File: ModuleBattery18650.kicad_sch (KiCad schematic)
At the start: 28 parts, among them J1 Connector_6p, T1 SI2323DS-T1-E3, T2 FDN337N, T3 SI2323DS-T1-E3, U1 MCP73832-2-OT, U2 MCP121T-315E

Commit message: Changes
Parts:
- removed C1: 4.7uF, 0ESN_Lib:C_0805_2012Metric_Pad1.18x1.45mm_HandSolder, symbol Device:C
- removed D1: LED 2V, 0ESN_Lib:D_0603_1608Metric_Pad1.05x0.95mm_HandSolder, symbol Device:LED
- removed JP1, JP2: Jumper_2_Bridged, 0ESN_Lib:PinHeader_1x02_P1.27mm_Vertical, symbol 0ESN_Lib:Jumper_2_Bridged
- removed R2: 1k8, 0ESN_Lib:R_0603_1608Metric_Pad0.98x0.95mm_HandSolder, symbol Device:R
- removed R3: 4k7, 0ESN_Lib:R_0603_1608Metric_Pad0.98x0.95mm_HandSolder, symbol Device:R
- removed U1: MCP73832-2-OT, 0ESN_Lib:SOT-23-5_HandSoldering, symbol 0ESN_Lib:MCP73832-2-OT
- added RS1: 0R NP, 0ESN_Lib:R_0603_1608Metric_Pad0.98x0.95mm_HandSolder, symbol Device:R
- added T1, T2: SI2323DS, Package_TO_SOT_SMD:SOT-23_Handsoldering, symbol 0ESN_Lib:SI2323DS
- added TP9: TestPoint, 0ESN_Lib:TestPoint_Pad_D1.0mm, symbol 0ESN_Lib:TestPoint
- R1: value 3k9 -> 1M
- T4: renamed from T3; value SI2323DS-T1-E3 -> SI2323DS; symbol 0ESN_Lib:SI2323DS-T1-E3 -> 0ESN_Lib:SI2323DS
- T5: renamed from T1; value SI2323DS-T1-E3 -> SI2323DS; symbol 0ESN_Lib:SI2323DS-T1-E3 -> 0ESN_Lib:SI2323DS
- renumbered C2 to C1, JP3 to JP1, R4 to R2, R5 to R3, R6 to RS2, T2 to T3, TP4 to TP2, TP2 to TP4, U2 to U1
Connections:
- net VDD is gone; now on an unnamed net: JP1.2 (B), TP3.1
- net GND: now also T1.1 (G)
- net Vbat: now also T5.2 (S), TP9.1; no longer RS2.2, T4.3 (D), TP8.1
- net at R2.1, R3.1, RS2.1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: now also RS1.2, T2.3 (D); no longer T5.2 (S)
- net at R1.1: now also T1.3 (D), T2.1 (G)
- net Vcharge: no longer names the net of C1.1, F1.2, TP4.1
- net Vcharge: now also RS1.1, T1.2 (S), T2.2 (S); no longer T5.3 (D)
- new net: RS2.2, T4.3 (D), T5.3 (D), TP8.1
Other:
- note added: "Bypass resistor"
- note added: "Disable subcircuit when charging"
- note added: "Prevent over-discharge"
- note added: "Prevent reverse current"
- note added: "Replace with different pins one 1x Vbat 1x Vcharge 1x GND"
- note added: "Using 3 P-Channel mosfet adds a serial resistor to the battery The SI2323DS has a Rds_on of about 39 mOhm with this voltage A better one like the SI7145DP has a Rds_on of up to 6 mOhm for 3V Or the SISH615ADN for a cheaper alternative, Rds_on up to 8 mOhm A serial resistance of 120 mOhm would mean that drawing 1 Amp from the current source, 120mW is dissiped into the mosfets"
- note added: "When over-discharge disabled : MCP121T consumes 1.75 uA R1 draws nothing R2 draws nothing R3 draws 3.08 uA Total is around 5 uA"
- note added: "When over-discharge enabled : MCP121T consumes 1.75 uA R1 draws nothing R2 draws 3.08 uA (for 1 Mohm, need to verify that is enough to pull up T3) R3 draws nothing as the gate of T4 is High Total is around 5 uA"
- note removed: "256mA"
- note removed: "555mA"
- note removed: "Ich = 1000V/Rch [A]"
- moved on the sheet: J1, JP1, R2, R3, RS2, T3, T4, T5, TP1, TP2, TP3, TP4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

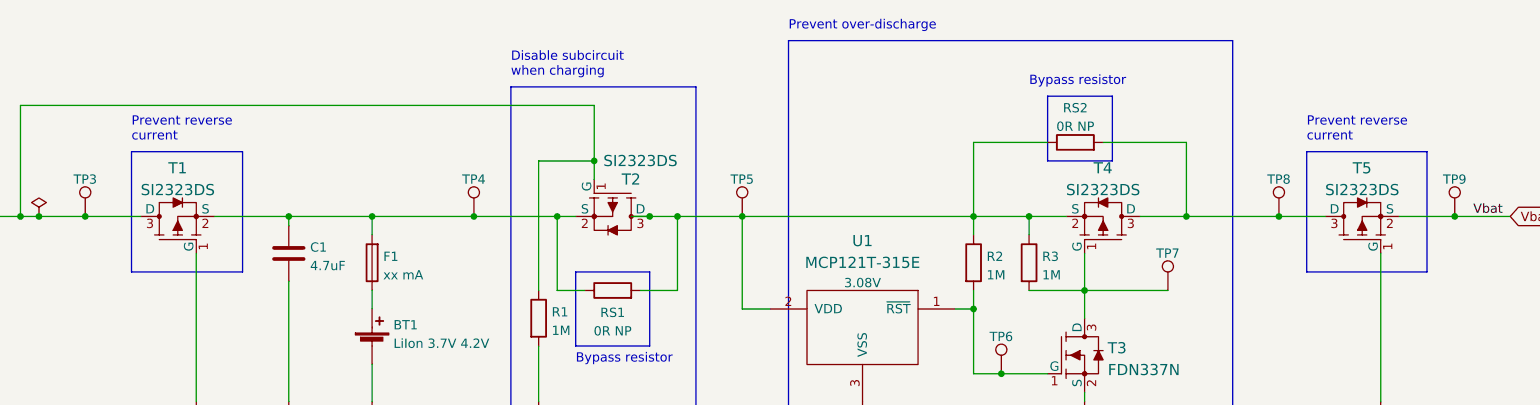
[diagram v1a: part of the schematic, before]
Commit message: corrected mosfet model
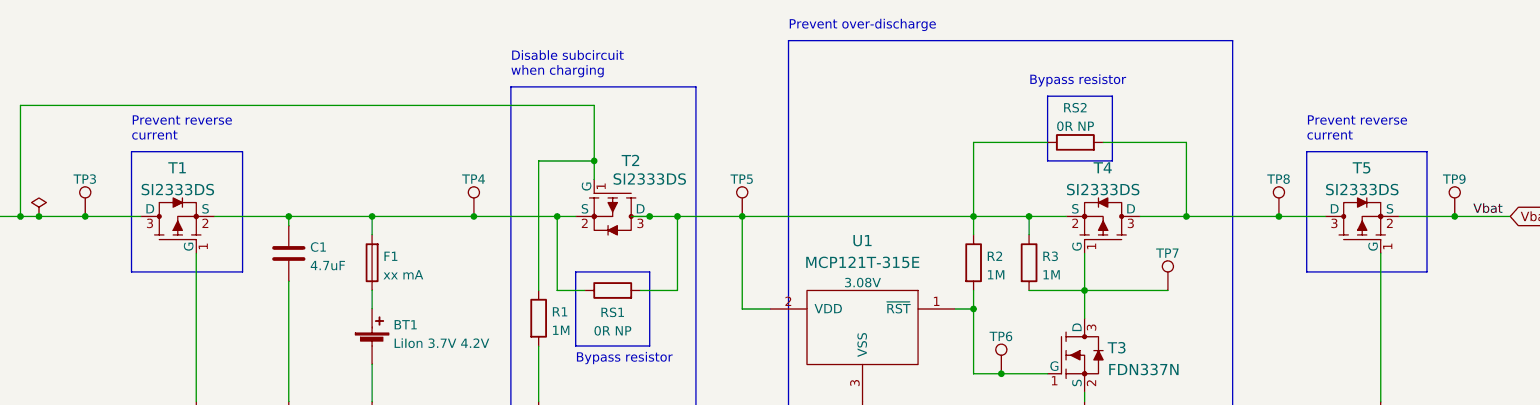
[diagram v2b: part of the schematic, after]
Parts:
- T1, T2, T4, T5: value SI2323DS -> SI2333DS; symbol 0ESN_Lib:SI2323DS -> 0ESN_Lib:SI2333DS
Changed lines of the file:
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@@
   (symbol (lib_id "power:GND") (at 256.54 83.82 0) (unit 1)
     (in_bom yes) (on_board yes) (fields_autoplaced)
-    (property "Reference" "#PWR010" (id 0) (at 256.54 90.17 0)
+    (property "Reference" "#PWR08" (id 0) (at 256.54 90.17 0)
       (effects (font (size 1.27 1.27)) hide)
     )
@@
     (pin "1")
   )
-  (symbol (lib_id "0ESN_Lib:SI2323DS") (at 91.44 58.42 0) (unit 1)
+  (symbol (lib_id "0ESN_Lib:SI2333DS") (at 91.44 58.42 0) (unit 1)
     (in_bom yes) (on_board yes) (fields_autoplaced)
     (property "Reference" "T1" (id 0) (at 91.44 51.7959 0)
       (effects (font (size 1.524 1.524)))
     )
-    (property "Value" "SI2323DS" (id 1) (at 91.44 54.7893 0)
+    (property "Value" "SI2333DS" (id 1) (at 91.44 54.7893 0)
       (effects (font (size 1.524 1.524)))
     )
@@
       (effects (font (size 1.524 1.524)) hide)
     )
-    (property "Datasheet" "" (id 3) (at 91.44 59.055 0)
+    (property "Datasheet" "https://www.vishay.com/docs/72023/72023.pdf" (id 3) (at 91.44 59.055 0)
       (effects (font (size 1.524 1.524)) hide)
     )
@@
   (symbol (lib_id "power:GND") (at 93.98 83.82 0) (unit 1)
     (in_bom yes) (on_board yes) (fields_autoplaced)
-    (property "Reference" "#PWR03" (id 0) (at 93.98 90.17 0)
+    (property "Reference" "#PWR02" (id 0) (at 93.98 90.17 0)
       (effects (font (size 1.27 1.27)) hide)
     )
@@
     (pin "1")
   )
-  (symbol (lib_id "0ESN_Lib:SI2323DS") (at 151.13 58.42 180) (unit 1)
+  (symbol (lib_id "0ESN_Lib:SI2333DS") (at 151.13 58.42 180) (unit 1)
     (in_bom yes) (on_board yes)
-    (property "Reference" "T2" (id 0) (at 153.67 53.34 0)
-      (effects (font (size 1.524 1.524)))
-    )
-    (property "Value" "SI2323DS" (id 1) (at 154.94 50.8 0)
+    (property "Reference" "T2" (id 0) (at 153.67 50.8 0)
+      (effects (font (size 1.524 1.524)))
+    )
+    (property "Value" "SI2333DS" (id 1) (at 156.21 53.34 0)
       (effects (font (size 1.524 1.524)))
     )
@@
       (effects (font (size 1.524 1.524)) hide)
     )
-    (property "Datasheet" "" (id 3) (at 151.13 57.785 0)
+    (property "Datasheet" "https://www.vishay.com/docs/72023/72023.pdf" (id 3) (at 151.13 57.785 0)
       (effects (font (size 1.524 1.524)) hide)
     )
@@
     (pin "1")
   )
-  (symbol (lib_id "0ESN_Lib:SI2323DS") (at 254 58.42 0) (unit 1)
+  (symbol (lib_id "0ESN_Lib:SI2333DS") (at 254 58.42 0) (unit 1)
     (in_bom yes) (on_board yes) (fields_autoplaced)
     (property "Reference" "T5" (id 0) (at 254 51.7959 0)
       (effects (font (size 1.524 1.524)))
     )
-    (property "Value" "SI2323DS" (id 1) (at 254 54.7893 0)
+    (property "Value" "SI2333DS" (id 1) (at 254 54.7893 0)
       (effects (font (size 1.524 1.524)))
     )
@@
       (effects (font (size 1.524 1.524)) hide)
     )
-    (property "Datasheet" "" (id 3) (at 254 59.055 0)
+    (property "Datasheet" "https://www.vishay.com/docs/72023/72023.pdf" (id 3) (at 254 59.055 0)
       (effects (font (size 1.524 1.524)) hide)
     )
@@
   (symbol (lib_id "power:GND") (at 140.97 83.82 0) (unit 1)
     (in_bom yes) (on_board yes) (fields_autoplaced)
-    (property "Reference" "#PWR06" (id 0) (at 140.97 90.17 0)
+    (property "Reference" "#PWR05" (id 0) (at 140.97 90.17 0)
       (effects (font (size 1.27 1.27)) hide)
     )
@@
   (symbol (lib_id "power:GND") (at 106.68 83.82 0) (unit 1)
     (in_bom yes) (on_board yes) (fields_autoplaced)
-    (property "Reference" "#PWR04" (id 0) (at 106.68 90.17 0)
+    (property "Reference" "#PWR03" (id 0) (at 106.68 90.17 0)
       (effects (font (size 1.27 1.27)) hide)
     )
@@
   (symbol (lib_id "power:GND") (at 215.9 83.82 0) (unit 1)
     (in_bom yes) (on_board yes) (fields_autoplaced)
-    (property "Reference" "#PWR09" (id 0) (at 215.9 90.17 0)
+    (property "Reference" "#PWR07" (id 0) (at 215.9 90.17 0)
       (effects (font (size 1.27 1.27)) hide)
     )
@@
   (symbol (lib_id "power:GND") (at 185.42 83.82 0) (unit 1)
     (in_bom yes) (on_board yes) (fields_autoplaced)
-    (property "Reference" "#PWR08" (id 0) (at 185.42 90.17 0)
+    (property "Reference" "#PWR06" (id 0) (at 185.42 90.17 0)
       (effects (font (size 1.27 1.27)) hide)
     )
@@
   (symbol (lib_id "power:GND") (at 118.11 83.82 0) (unit 1)
     (in_bom yes) (on_board yes) (fields_autoplaced)
-    (property "Reference" "#PWR05" (id 0) (at 118.11 90.17 0)
+    (property "Reference" "#PWR04" (id 0) (at 118.11 90.17 0)
       (effects (font (size 1.27 1.27)) hide)
     )
@@
     (pin "1")
   )
-  (symbol (lib_id "0ESN_Lib:SI2323DS") (at 218.44 58.42 0) (mirror y) (unit 1)
+  (symbol (lib_id "0ESN_Lib:SI2333DS") (at 218.44 58.42 0) (mirror y) (unit 1)
     (in_bom yes) (on_board yes) (fields_autoplaced)
     (property "Reference" "T4" (id 0) (at 218.44 51.7959 0)
       (effects (font (size 1.524 1.524)))
     )
-    (property "Value" "SI2323DS" (id 1) (at 218.44 54.7893 0)
+    (property "Value" "SI2333DS" (id 1) (at 218.44 54.7893 0)
       (effects (font (size 1.524 1.524)))
     )
@@
       (effects (font (size 1.524 1.524)) hide)
     )
-    (property "Datasheet" "" (id 3) (at 218.44 59.055 0)
+    (property "Datasheet" "https://www.vishay.com/docs/72023/72023.pdf" (id 3) (at 218.44 59.055 0)
       (effects (font (size 1.524 1.524)) hide)
     )
@@
     )
     (path "/23b85cef-66d9-43b8-b31f-1044e0d3ebc7"
+      (reference "#PWR02") (unit 1) (value "GND") (footprint "")
+    )
+    (path "/a1c2006c-9990-442c-88d7-ddca560a04cd"
       (reference "#PWR03") (unit 1) (value "GND") (footprint "")
     )
-    (path "/a1c2006c-9990-442c-88d7-ddca560a04cd"
+    (path "/e065cd76-3830-4be0-892c-04089454b25f"
       (reference "#PWR04") (unit 1) (value "GND") (footprint "")
     )
-    (path "/e065cd76-3830-4be0-892c-04089454b25f"
+    (path "/60ef1753-16ee-40fd-a34a-5fee75f98232"
       (reference "#PWR05") (unit 1) (value "GND") (footprint "")
     )
-    (path "/60ef1753-16ee-40fd-a34a-5fee75f98232"
+    (path "/cfa2cdea-57ac-4cf2-a8c7-f359f96a51ae"
       (reference "#PWR06") (unit 1) (value "GND") (footprint "")
     )
-    (path "/cfa2cdea-57ac-4cf2-a8c7-f359f96a51ae"
+    (path "/c5589686-1dea-4bbf-935c-6a54f89cec88"
+      (reference "#PWR07") (unit 1) (value "GND") (footprint "")
+    )
+    (path "/0fa377f7-81c1-4b1f-8399-5259acb98d09"
       (reference "#PWR08") (unit 1) (value "GND") (footprint "")
-    )
-    (path "/c5589686-1dea-4bbf-935c-6a54f89cec88"
-      (reference "#PWR09") (unit 1) (value "GND") (footprint "")
-    )
-    (path "/0fa377f7-81c1-4b1f-8399-5259acb98d09"
-      (reference "#PWR010") (unit 1) (value "GND") (footprint "")
     )
     (path "/3563b52b-d2c0-41b9-aeca-2af682e9e33e"
@@
     )
     (path "/1faa3af5-61f3-4f40-a3ca-42ba69cf237c"
-      (reference "T1") (unit 1) (value "SI2323DS") (footprint "Package_TO_SOT_SMD:SOT-23_Handsoldering")
+      (reference "T1") (unit 1) (value "SI2333DS") (footprint "Package_TO_SOT_SMD:SOT-23_Handsoldering")
     )
     (path "/314eb51e-b3ac-4ba9-8b88-2b7ab2de42c3"
-      (reference "T2") (unit 1) (value "SI2323DS") (footprint "Package_TO_SOT_SMD:SOT-23_Handsoldering")
+      (reference "T2") (unit 1) (value "SI2333DS") (footprint "Package_TO_SOT_SMD:SOT-23_Handsoldering")
     )
     (path "/78dd3410-41be-43bf-b6a5-ead893855ad4"
@@
     )
     (path "/f948391d-3a89-47b0-b2ec-af1ff0696bd4"
-      (reference "T4") (unit 1) (value "SI2323DS") (footprint "Package_TO_SOT_SMD:SOT-23_Handsoldering")
+      (reference "T4") (unit 1) (value "SI2333DS") (footprint "Package_TO_SOT_SMD:SOT-23_Handsoldering")
     )
     (path "/57796aa7-6c40-491b-8224-cb866b640d9f"
-      (reference "T5") (unit 1) (value "SI2323DS") (footprint "Package_TO_SOT_SMD:SOT-23_Handsoldering")
+      (reference "T5") (unit 1) (value "SI2333DS") (footprint "Package_TO_SOT_SMD:SOT-23_Handsoldering")
     )
     (path "/fec7520f-6d3f-4e1d-a13a-d895d7868e2f"

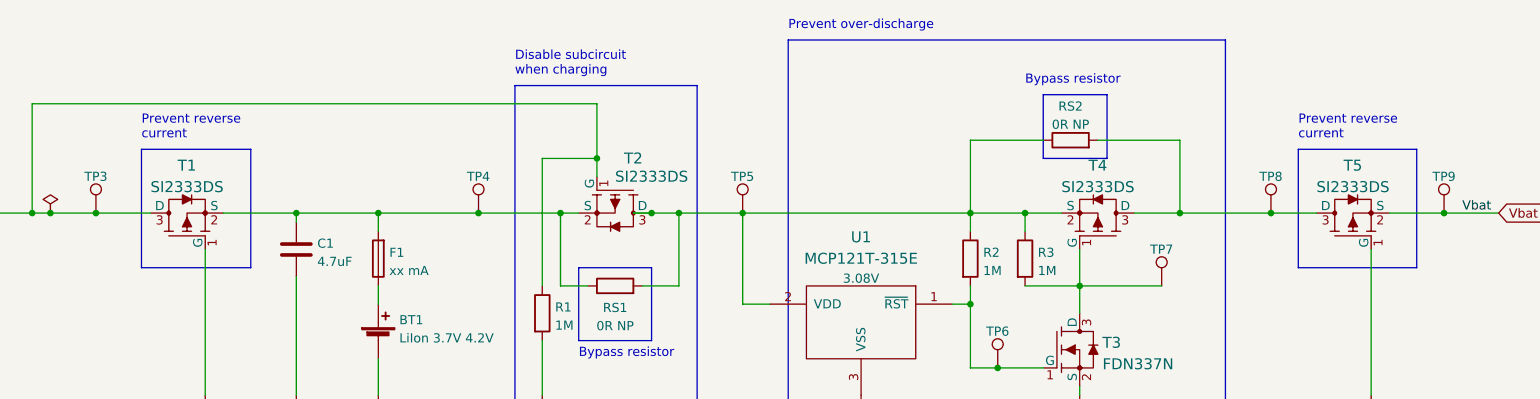
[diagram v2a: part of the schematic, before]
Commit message: Changed mosfets models to SISH615ADN
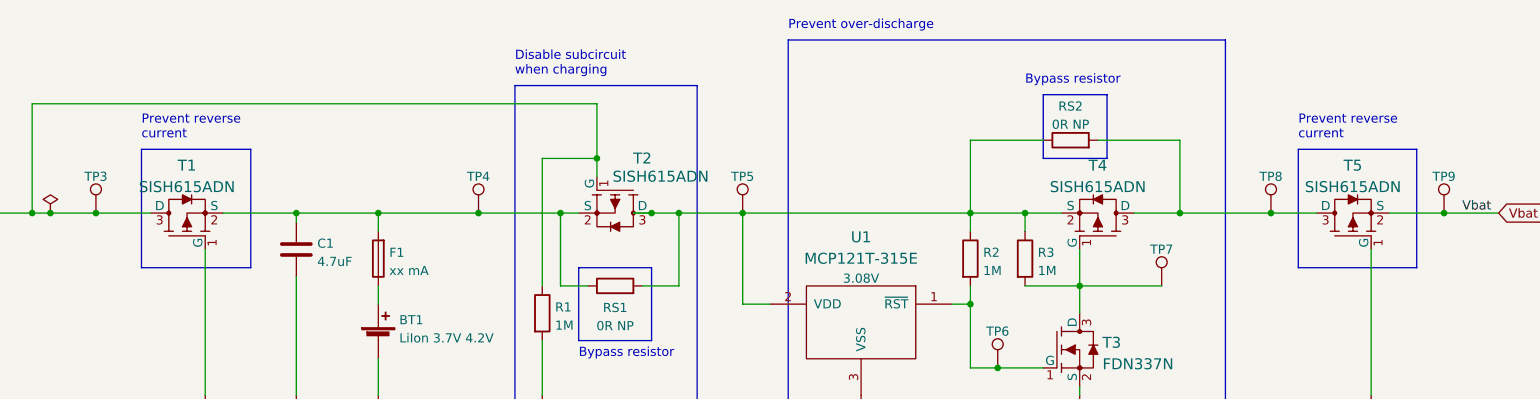
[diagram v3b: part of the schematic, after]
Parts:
- T1, T2, T4, T5: value SI2333DS -> SISH615ADN; footprint Package_TO_SOT_SMD:SOT-23_Handsoldering -> 0ESN_Lib:PowerPAK 1212-8S; symbol 0ESN_Lib:SI2333DS -> 0ESN_Lib:SISH615ADN
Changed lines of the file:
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@@
     (pin "1")
   )
-  (symbol (lib_id "0ESN_Lib:SI2333DS") (at 91.44 58.42 0) (unit 1)
+  (symbol (lib_id "0ESN_Lib:SISH615ADN") (at 91.44 58.42 0) (unit 1)
     (in_bom yes) (on_board yes) (fields_autoplaced)
     (property "Reference" "T1" (id 0) (at 91.44 51.7959 0)
       (effects (font (size 1.524 1.524)))
     )
-    (property "Value" "SI2333DS" (id 1) (at 91.44 54.7893 0)
-      (effects (font (size 1.524 1.524)))
-    )
-    (property "Footprint" "Package_TO_SOT_SMD:SOT-23_Handsoldering" (id 2) (at 91.44 59.055 0)
+    (property "Value" "SISH615ADN" (id 1) (at 91.44 54.7893 0)
+      (effects (font (size 1.524 1.524)))
+    )
+    (property "Footprint" "0ESN_Lib:PowerPAK 1212-8S" (id 2) (at 91.44 59.055 0)
       (effects (font (size 1.524 1.524)) hide)
     )
@@
     (pin "1")
   )
-  (symbol (lib_id "0ESN_Lib:SI2333DS") (at 151.13 58.42 180) (unit 1)
+  (symbol (lib_id "0ESN_Lib:SISH615ADN") (at 151.13 58.42 180) (unit 1)
     (in_bom yes) (on_board yes)
-    (property "Reference" "T2" (id 0) (at 153.67 50.8 0)
-      (effects (font (size 1.524 1.524)))
-    )
-    (property "Value" "SI2333DS" (id 1) (at 156.21 53.34 0)
-      (effects (font (size 1.524 1.524)))
-    )
-    (property "Footprint" "Package_TO_SOT_SMD:SOT-23_Handsoldering" (id 2) (at 151.13 57.785 0)
+    (property "Reference" "T2" (id 0) (at 154.94 50.8 0)
+      (effects (font (size 1.524 1.524)))
+    )
+    (property "Value" "SISH615ADN" (id 1) (at 157.48 53.34 0)
+      (effects (font (size 1.524 1.524)))
+    )
+    (property "Footprint" "0ESN_Lib:PowerPAK 1212-8S" (id 2) (at 151.13 57.785 0)
       (effects (font (size 1.524 1.524)) hide)
     )
@@
     (pin "1")
   )
-  (symbol (lib_id "0ESN_Lib:SI2333DS") (at 254 58.42 0) (unit 1)
+  (symbol (lib_id "0ESN_Lib:SISH615ADN") (at 254 58.42 0) (unit 1)
     (in_bom yes) (on_board yes) (fields_autoplaced)
     (property "Reference" "T5" (id 0) (at 254 51.7959 0)
       (effects (font (size 1.524 1.524)))
     )
-    (property "Value" "SI2333DS" (id 1) (at 254 54.7893 0)
-      (effects (font (size 1.524 1.524)))
-    )
-    (property "Footprint" "Package_TO_SOT_SMD:SOT-23_Handsoldering" (id 2) (at 254 59.055 0)
+    (property "Value" "SISH615ADN" (id 1) (at 254 54.7893 0)
+      (effects (font (size 1.524 1.524)))
+    )
+    (property "Footprint" "0ESN_Lib:PowerPAK 1212-8S" (id 2) (at 254 59.055 0)
       (effects (font (size 1.524 1.524)) hide)
     )
@@
     (pin "1")
   )
-  (symbol (lib_id "0ESN_Lib:SI2333DS") (at 218.44 58.42 0) (mirror y) (unit 1)
+  (symbol (lib_id "0ESN_Lib:SISH615ADN") (at 218.44 58.42 0) (mirror y) (unit 1)
     (in_bom yes) (on_board yes) (fields_autoplaced)
     (property "Reference" "T4" (id 0) (at 218.44 51.7959 0)
       (effects (font (size 1.524 1.524)))
     )
-    (property "Value" "SI2333DS" (id 1) (at 218.44 54.7893 0)
-      (effects (font (size 1.524 1.524)))
-    )
-    (property "Footprint" "Package_TO_SOT_SMD:SOT-23_Handsoldering" (id 2) (at 218.44 59.055 0)
+    (property "Value" "SISH615ADN" (id 1) (at 218.44 54.7893 0)
+      (effects (font (size 1.524 1.524)))
+    )
+    (property "Footprint" "0ESN_Lib:PowerPAK 1212-8S" (id 2) (at 218.44 59.055 0)
       (effects (font (size 1.524 1.524)) hide)
     )
@@
     )
     (path "/1faa3af5-61f3-4f40-a3ca-42ba69cf237c"
-      (reference "T1") (unit 1) (value "SI2333DS") (footprint "Package_TO_SOT_SMD:SOT-23_Handsoldering")
+      (reference "T1") (unit 1) (value "SISH615ADN") (footprint "0ESN_Lib:PowerPAK 1212-8S")
     )
     (path "/314eb51e-b3ac-4ba9-8b88-2b7ab2de42c3"
-      (reference "T2") (unit 1) (value "SI2333DS") (footprint "Package_TO_SOT_SMD:SOT-23_Handsoldering")
+      (reference "T2") (unit 1) (value "SISH615ADN") (footprint "0ESN_Lib:PowerPAK 1212-8S")
     )
     (path "/78dd3410-41be-43bf-b6a5-ead893855ad4"
@@
     )
     (path "/f948391d-3a89-47b0-b2ec-af1ff0696bd4"
-      (reference "T4") (unit 1) (value "SI2333DS") (footprint "Package_TO_SOT_SMD:SOT-23_Handsoldering")
+      (reference "T4") (unit 1) (value "SISH615ADN") (footprint "0ESN_Lib:PowerPAK 1212-8S")
     )
     (path "/57796aa7-6c40-491b-8224-cb866b640d9f"
-      (reference "T5") (unit 1) (value "SI2333DS") (footprint "Package_TO_SOT_SMD:SOT-23_Handsoldering")
+      (reference "T5") (unit 1) (value "SISH615ADN") (footprint "0ESN_Lib:PowerPAK 1212-8S")
     )
     (path "/fec7520f-6d3f-4e1d-a13a-d895d7868e2f"

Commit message: adapted footprints
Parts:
- removed J1: Connector_6p, 0ESN_Lib:Connector_6p_m, symbol 0ESN_Lib:Connector_6p
- added J1: Connector_2p, 0ESN_Lib:Connector_2p_m, symbol 0ESN_Lib:Connector_2p
- added J2: Connector_2p_r, 0ESN_Lib:Connector_2p_m, symbol 0ESN_Lib:Connector_2p_r
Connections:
- net GND: now also J1.2 (P2), J2.2 (P2)
- net Vbat: now also J2.1 (P1)
- net Vch: now also J1.1 (P1)
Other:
- moved on the sheet: T5, TP8, TP9
